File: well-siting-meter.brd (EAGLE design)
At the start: 100 x 80 mm, 27 parts, among them J2 7805

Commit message: boost circuit, lcd screen, starting board layout
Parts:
- removed J3, J4, J5: (no value), SparkFun-Connectors:SCREWTERMINAL-5MM-2
- removed JP1: JUMPER-PAD-2-NO, SparkFun-Passives:PAD-JUMPER-2-NO_NO_SILK
- removed U$1, U$2: EC2, ec2:EC2
- removed U$3: ARDUINO_PRO_MINI, SparkFun-Boards:ARDUINO_PRO_MINI
- removed U$4, U$5: AD623, ad623:AD623
- removed U$6: DF2X, df2x:4-EDIP
- added FRAME1: FRAME-LETTER, SparkFun-Aesthetics:CREATIVE_COMMONS
- added J10, J11, J12, J7, J8, J9: (no value), SparkFun-Connectors:BANANA_CONN
- added U1: LCD-16X2NOHOLES, SparkFun-Displays:LCD-16X2_NOHOLES
- added U2: ARDUINO_PRO_MINI, SparkFun-Boards:ARDUINO_PRO_MINI
- added U3, U4: EC2, ec2:EC2
- added U5, U6: AD623, ad623:AD623
- C1: value (none) -> 150uF
- C6, C7: value 10uf -> 10uF
- J1: value (none) -> MC34063HV; device SparkFun-Connectors:1X06 -> mc34063hv:MC34063HV
- J6: value (none) -> BTN; device SparkFun-Connectors:SCREWTERMINAL-5MM-3 -> SparkFun-Connectors:1X03
- R1, R2, R3, R4: value (none) -> 10K
- R5: value (none) -> 1.02K
- R6: value (none) -> 11K
- R7: value (none) -> 1
- moved C6 235.9 mm to (33.0, 69.8)
- moved C7 235.9 mm to (36.8, 69.8)
- moved J2 228.5 mm to (25.9, 69.3)
- moved R6 200.4 mm to (35.6, 59.7), turned to 90 degrees
- moved R4 191.1 mm to (18.8, 65.3), turned to 180 degrees
- moved R1 184.0 mm to (53.3, 59.7), turned to 270 degrees
- moved R5 182.5 mm to (35.6, 45.7), turned to 90 degrees
- moved R7 182.3 mm to (30.5, 36.8)
- moved R2 176.2 mm to (53.3, 45.7), turned to 270 degrees
- moved R3 172.9 mm to (19.1, 51.3), turned to 180 degrees
- moved J6 158.2 mm to (17.8, 69.8)
- moved J1 116.1 mm to (53.3, 29.2), turned to 180 degrees
- moved D2 108.5 mm to (7.62, 59.7), turned to 90 degrees
- moved C1 100.1 mm to (13.0, 34.3), turned to 180 degrees
- moved Q2 98.6 mm to (3.81, 59.7), turned to 90 degrees
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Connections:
- removed net G: J6.1, JP1.2
- removed net L: J6.3, U$6.2
- removed net N: J6.2, U$6.3
- removed net RXD: J1.5, U$3.15
- removed net STATE: J1.6, U$3.13
- removed net TXD: J1.4, U$3.14
- new net DB4: U1.11
- new net DB5: U1.12
- new net DB6: U1.13
- new net DB7: U1.14
- new net E: U1.6
- new net RS: U1.4
- new net VO: U1.3
- net 5V: now also U1.15, U1.2, U2.21, U5.7, U6.7; no longer J1.2, U$3.21, U$4.7, U$5.7
- net EN: now also U2.16; no longer J1.1, U$3.16
- net GND: now also J1.P$2, J1.P$4, J6.1, J8.P$1, U1.1, U1.16, U1.5, U2.4, U5.2, U5.4, U6.4; no longer J1.3, J3.1, JP1.1, U$3.4, U$4.4, U$5.4, U$6.4
- net I1: now also J9.P$1, U3.9; no longer J4.1, U$1.9
- net I2: now also J10.P$1, U3.4; no longer J4.2, U$1.4
- net IOUT: now also U2.17, U5.6; no longer U$3.17, U$4.6
- net IRET: now also U3.3, U3.8, U5.3; no longer U$1.3, U$1.8, U$4.3
- net ISW: now also U2.5; no longer U$3.5
- net N$1: now also U4.12; no longer U$2.12
- net N$24: now also U5.1; no longer U$4.1
- net N$25: now also U5.8; no longer U$4.8
- net N$26: now also U6.1; no longer U$5.1
- net N$27: now also U6.8; no longer U$5.8
- net N$4: now also U3.12; no longer U$1.12
- net V+: now also U4.10, U4.5, U6.3; no longer U$2.10, U$2.5, U$5.3
- net V-: now also U4.3, U4.8, U6.2; no longer U$2.3, U$2.8, U$5.2
- net V1: now also J11.P$1, U4.9; no longer J5.1, U$2.9
- net V2: now also J12.P$1, U4.4; no longer J5.2, U$2.4
- net VIN: now also J1.P$3, U3.10, U3.5; no longer U$1.10, U$1.5, U$6.1
- net VOUT: now also U2.18, U6.6; no longer U$3.18, U$5.6
- net VREF: now also U5.5, U6.5; no longer U$4.5, U$5.5
- net VSW: now also U2.6; no longer U$3.6
- net V_BATT: now also J1.P$1, J7.P$1, U3.1, U4.1; no longer J3.2, U$1.1, U$2.1
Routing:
- net N$5: track 0.00 -> 16.8 mm
- net N$2: track 0.00 -> 16.6 mm
- net VIN: track 0.00 -> 16.1 mm
- net IRET: track 0.00 -> 13.5 mm
- net V_BATT: track 0.00 -> 12.3 mm
- net N$1: track 0.00 -> 11.5 mm
- net V-: track 0.00 -> 7.18 mm
- net V+: track 0.00 -> 7.18 mm
- net N$4: track 0.00 -> 6.13 mm
- net N$27: track 0.00 -> 3.81 mm
- net N$26: track 0.00 -> 3.81 mm
- net N$25: track 0.00 -> 3.81 mm
- net N$24: track 0.00 -> 3.81 mm
- added copper zone on layer 1, net 5V
- added copper zone on layer 16, net GND
- added copper zone on layer 1, net V_BATT
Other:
- board size 100 x 80 mm -> 103.9 x 76.1 mm

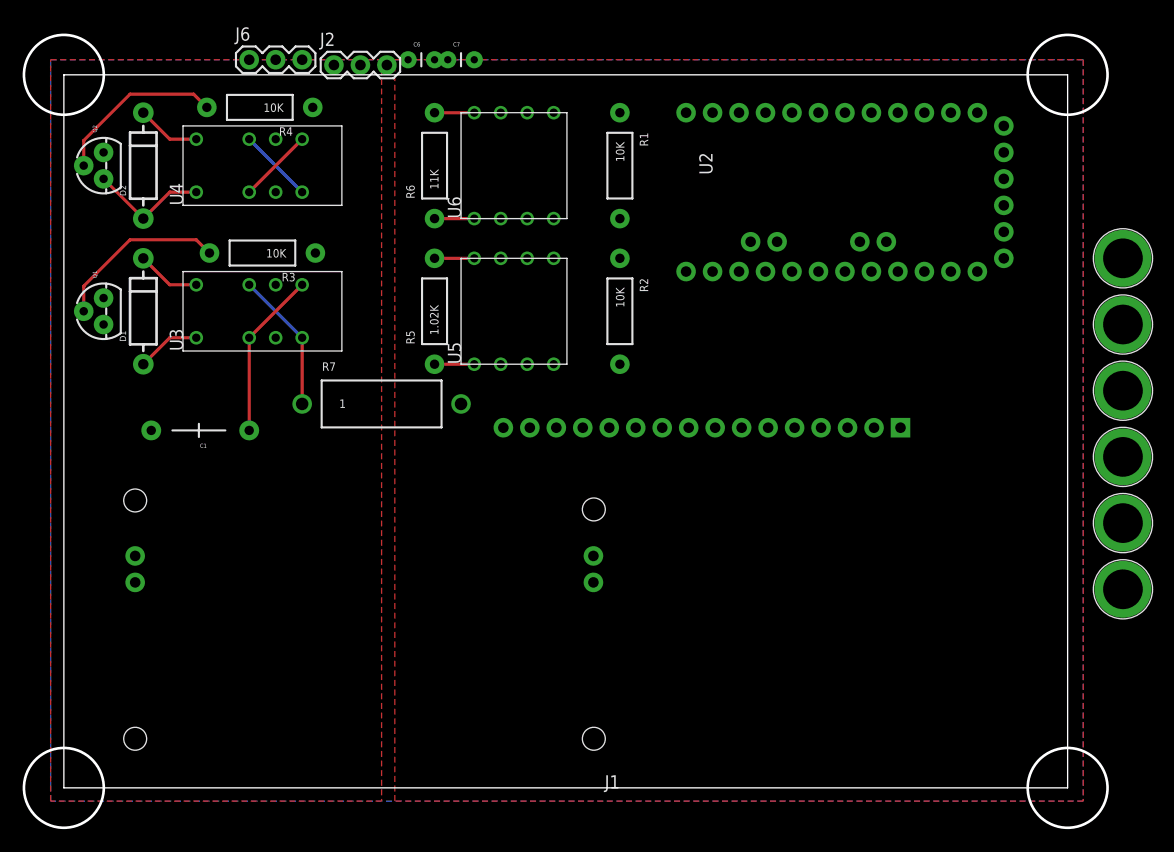
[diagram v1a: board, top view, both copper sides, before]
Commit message: "finished" design, but need to update boot circuity for > 10W max
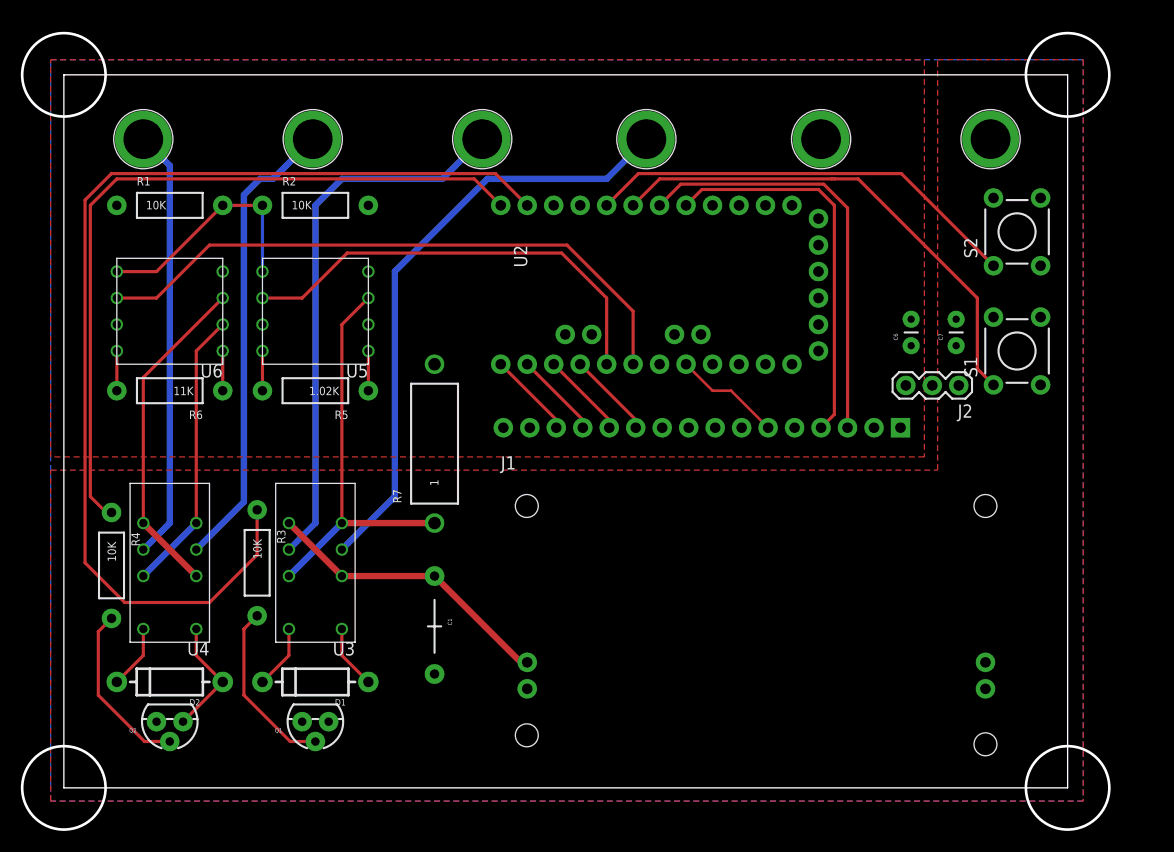
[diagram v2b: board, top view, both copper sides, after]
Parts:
- removed J6: BTN, SparkFun-Connectors:1X03
- added S1, S2: SWITCH-MOMENTARY-2PTH, SparkFun-Electromechanical:TACTILE-PTH
- moved J12 94.7 mm to (7.62, 62.2)
- moved J11 88.9 mm to (23.9, 62.2)
- moved J10 71.7 mm to (40.1, 62.2)
- moved J2 67.4 mm to (85.9, 38.6), turned to 180 degrees
- moved C7 56.0 mm to (85.6, 42.4), turned to 90 degrees
- moved C6 55.5 mm to (81.3, 42.4), turned to 90 degrees
- moved J9 54.9 mm to (55.9, 62.2)
- moved Q2 53.7 mm to (10.2, 6.35), turned to 180 degrees
- moved D2 49.6 mm to (10.2, 10.2), turned to 180 degrees
- moved R4 46.2 mm to (4.57, 21.3), turned to 270 degrees
- moved Q1 44.3 mm to (24.1, 6.35), turned to 180 degrees
- moved R1 43.3 mm to (10.2, 55.9), turned to 0 degrees
- moved D1 39.2 mm to (24.1, 10.2), turned to 180 degrees
- moved U4 39.1 mm to (10.2, 21.6), turned to 180 degrees
- moved J8 37.7 mm to (72.6, 62.2)
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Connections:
- removed net EN: U2.16
- new net B1: S1.1, U2.7
- new net B2: S2.1, U2.8
- net DB4: now also U2.16
- net DB5: now also U2.15
- net DB6: now also U2.14
- net DB7: now also U2.13
- net E: now also U2.20
- net GND: now also S1.3, S2.3; no longer J6.1
- net ISW: now also U2.11; no longer U2.5
- net RS: now also U2.5
- net VO: now also U2.6
- net VSW: now also U2.12; no longer U2.6
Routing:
- net ISW: track 0.00 -> 103.8 mm
- net VSW: track 0.00 -> 72.1 mm
- net VOUT: track 0.00 -> 59.3 mm
- net I1: track 0.00 -> 58.2 mm
- net I2: track 0.00 -> 52.7 mm
- net B1: track 0.00 -> 47.8 mm
- net V1: track 0.00 -> 44.7 mm
- net IOUT: track 0.00 -> 42.9 mm
- net B2: track 0.00 -> 42.0 mm
- net V2: track 0.00 -> 41.5 mm
- net VO: track 0.00 -> 40.9 mm
- net RS: track 0.00 -> 37.3 mm
- net IRET: track 13.5 -> 38.7 mm
- net V+: track 7.18 -> 31.9 mm
- net VREF: track 0.00 -> 23.0 mm
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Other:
- board size 103.9 x 76.1 mm -> 104.3 x 76.4 mm

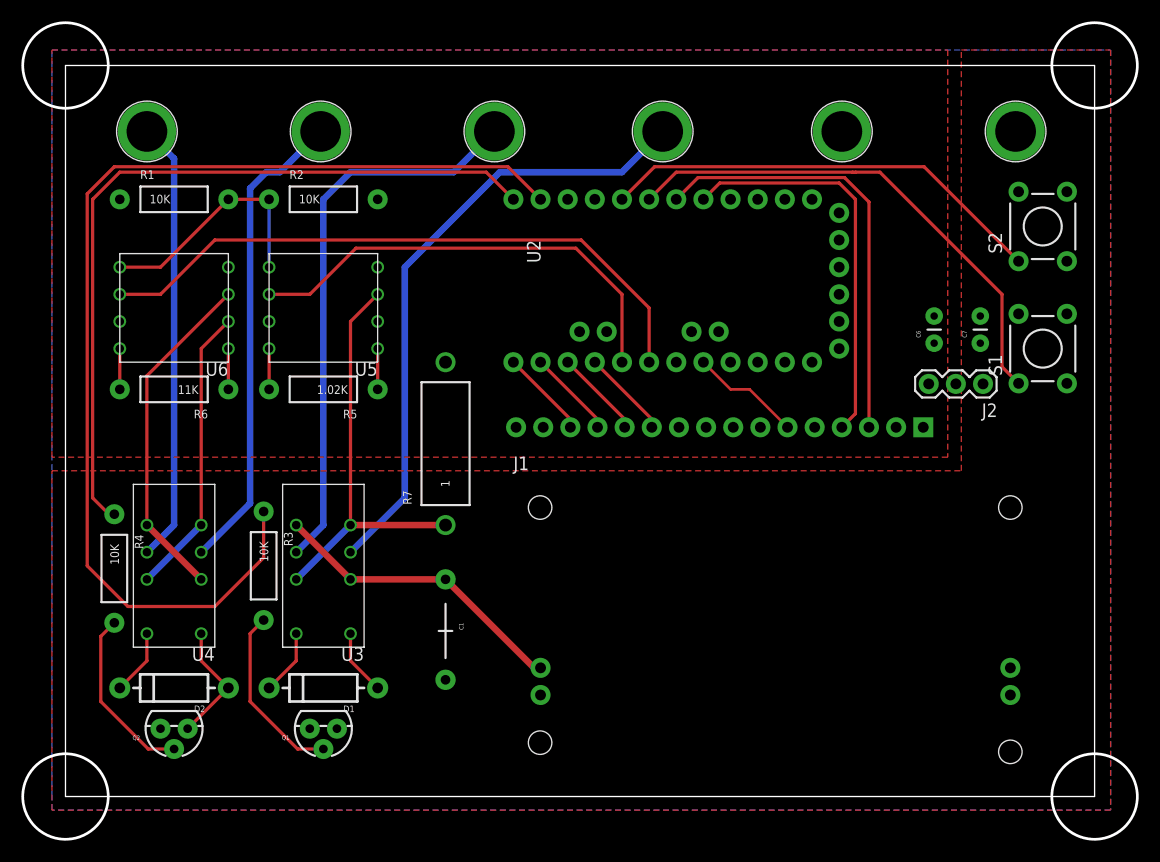
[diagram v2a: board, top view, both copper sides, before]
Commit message: added boost circuit
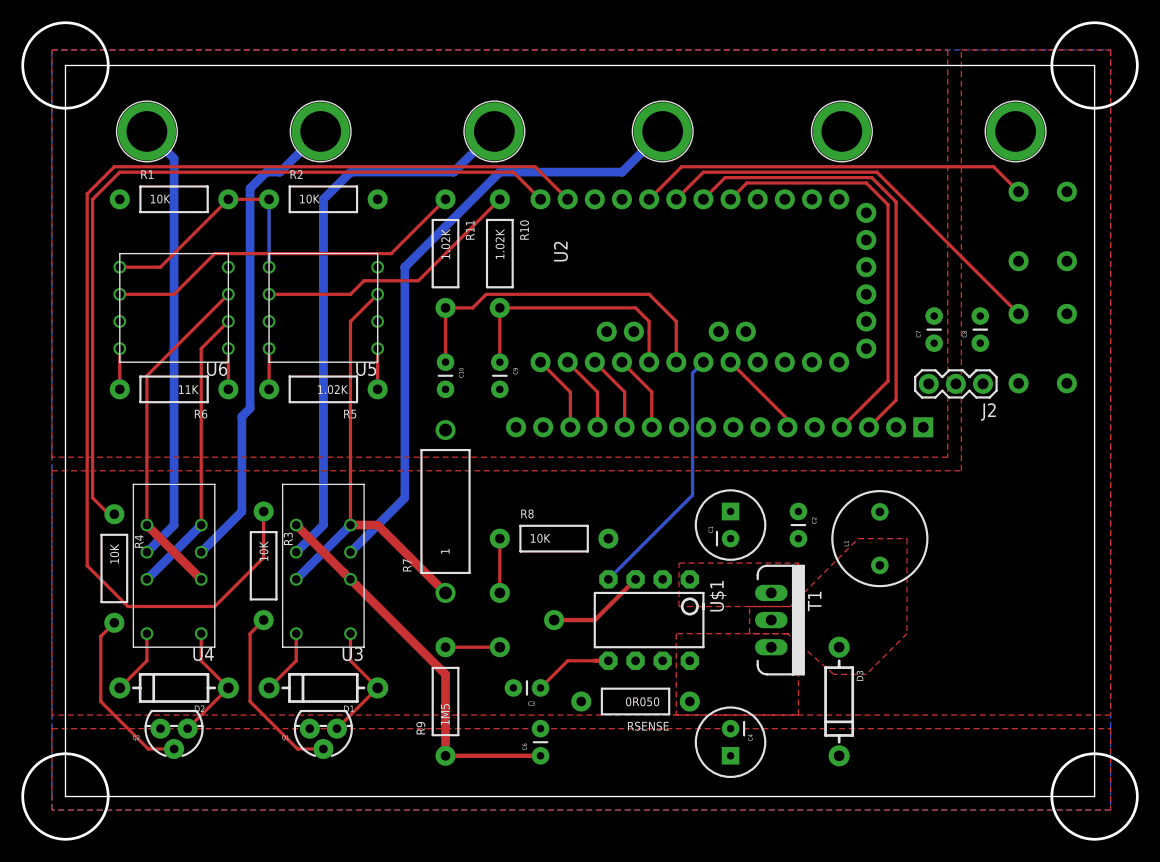
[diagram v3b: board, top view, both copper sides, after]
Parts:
- removed J1: MC34063HV, mc34063hv:MC34063HV
- added C10, C2, C3, C9: (no value), SparkFun-Passives:CAP-PTH-SMALL
- added C4: (no value), SparkFun-Passives:CPOL-RADIAL-100UF-25V
- added C8: 10uF, SparkFun-Passives:CAP-PTH-SMALL
- added D3: (no value), SparkFun-DiscreteSemi:DIODE-1N4001
- added L1: (no value), SparkFun-Passives:RLB0912
- added R10, R11: 1.02K, SparkFun-Passives:AXIAL-0.4
- added R8: 10K, SparkFun-Passives:AXIAL-0.4
- added R9: 1M5, SparkFun-Passives:AXIAL-0.4
- added RSENSE: 0R050, SparkFun-Passives:AXIAL-0.4
- added T1: MOSFET-NCHANNELFQP30N06L, SparkFun-DiscreteSemi:TO220V
- added U$1: MAX1771, max1771:DIP-08
- added VR1: 5K, SparkFun-Electromechanical:TRIM_POT
- C1: value 150uF -> (none); device SparkFun-Passives:CAP-PTH-LARGE -> SparkFun-Passives:CPOL-RADIAL-100UF-25V
- C6: value 10uF -> (none)
- moved C6 53.4 mm to (44.5, 3.81)
- moved C1 28.5 mm to (62.2, 25.4), turned to 90 degrees
- moved R7 6.35 mm to (35.6, 26.7)
- moved C7 4.32 mm to (81.3, 42.4)
- moved U2 2.54 mm to (59.7, 48.3)
- flipped S1 to the bottom, turned to 270 degrees
- flipped S2 to the bottom, turned to 270 degrees
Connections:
- new net N$10: T1.1, U$1.1
- new net N$11: RSENSE.P$1, T1.3, U$1.8
- new net N$12: R10.P$1, U5.6
- new net N$14: R11.P$1, U6.6
- new net N$15: U$1.3, VR1.1
- new net N$6: R9.P$2, VR1.3
- new net N$7: C3.1, U$1.5
- new net N$8: R8.P$1, VR1.2
- new net N$9: D3.A, L1.2, T1.2
- new net SHDN: U$1.4, U2.19
- net 5V: now also C7.1; no longer C6.1
- net GND: now also C10.2, C2.2, C3.2, C4.2, C8.2, C9.2, R8.P$2, RSENSE.P$2, U$1.6, U$1.7; no longer J1.P$2, J1.P$4
- net IOUT: now also C9.1, R10.P$2; no longer U5.6
- net VIN: now also C4.1, C6.1, D3.C, R9.P$1; no longer C1.1, J1.P$3
- net VOUT: now also C10.1, R11.P$2; no longer U6.6
- net V_BATT: now also C1.1, C2.1, C8.1, L1.1, U$1.2; no longer C7.1, J1.P$1
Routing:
- net N$14: track 0.00 -> 34.2 mm
- net VOUT: track 59.3 -> 32.1 mm
- net N$12: track 0.00 -> 25.3 mm
- net SHDN: track 0.00 -> 24.0 mm
- net IOUT: track 42.9 -> 23.4 mm
- net B1: track 47.8 -> 38.6 mm
- net N$15: track 0.00 -> 9.20 mm
- net VIN: track 28.4 -> 36.3 mm
- net N$7: track 0.00 -> 7.40 mm
- net N$4: track 6.13 -> 11.5 mm
- net B2: track 42.0 -> 36.8 mm
- net N$8: track 0.00 -> 5.08 mm
- net N$6: track 0.00 -> 5.08 mm
- net IRET: track 38.7 -> 41.3 mm
- net VSW: track 72.1 -> 74.6 mm
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- added copper zone on layer 1, net N$10
- added copper zone on layer 1, net N$11
- added copper zone on layer 1, net N$9
- added copper zone on layer 1, net VIN
